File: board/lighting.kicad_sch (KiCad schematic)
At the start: 2 parts, among them U3 SHHD003A0A

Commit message: Fan, Light, Buck
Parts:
- removed Conn2: Molex_SL_03, MRDT_Connectors:MOLEX_SL_03_Vertical, symbol MRDT_Connectors:Molex_SL_03
- removed U3: SHHD003A0A, MRDT_Devices:SHHD003A0A41Z_Through_Hole, symbol MRDT_Devices:SHHD003A0A
- added Conn10: Molex_SL_03, symbol MRDT_Connectors:Molex_SL_03
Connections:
- net GND: now also Conn10.3
- net NeoPixel: now also Conn10.2
- new net +5V: Conn10.1
- no-connect marks 1 -> 0
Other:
- note removed: "NeoPixels"

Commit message: Added most Footprints, Schematic review touch up
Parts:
- Conn10: footprint (none) -> MRDT_Connectors:MOLEX_SL_04_Vertical
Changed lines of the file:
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@@
 			)
 		)
-		(property "Footprint" ""
+		(property "Footprint" "MRDT_Connectors:MOLEX_SL_04_Vertical"
 			(at 106.68 87.63 0)
 			(effects

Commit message: Layout edits
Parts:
- Conn10: footprint MRDT_Connectors:MOLEX_SL_04_Vertical -> MRDT_Connectors:MOLEX_SL_03_Vertical
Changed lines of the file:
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@@
 			)
 		)
-		(property "Footprint" "MRDT_Connectors:MOLEX_SL_04_Vertical"
+		(property "Footprint" "MRDT_Connectors:MOLEX_SL_03_Vertical"
 			(at 106.68 87.63 0)
 			(effects

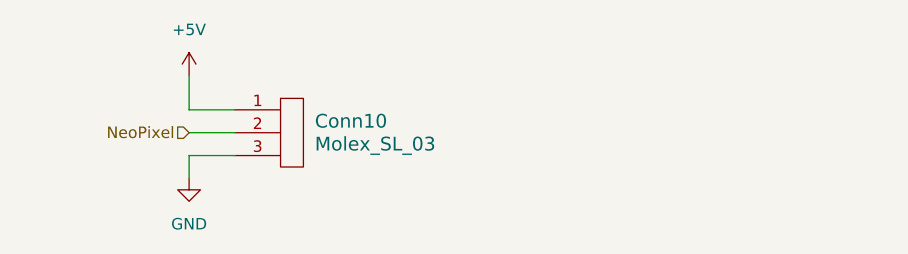
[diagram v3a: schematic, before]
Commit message: routed core board
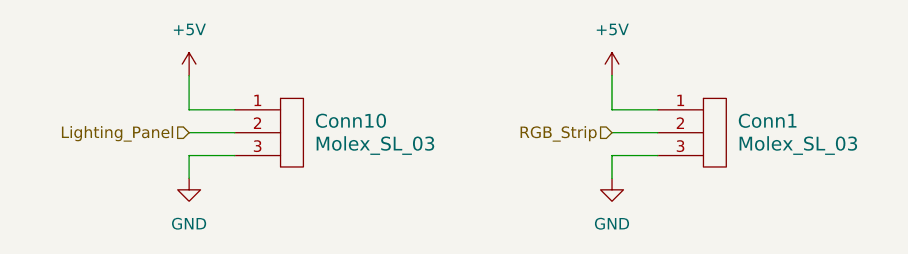
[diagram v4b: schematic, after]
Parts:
- added Conn1: Molex_SL_03, MRDT_Connectors:MOLEX_SL_03_Vertical, symbol MRDT_Connectors:Molex_SL_03
- Conn10: footprint MRDT_Connectors:MOLEX_SL_03_Vertical -> MRDT_Connectors:MOLEX_SL_03_Horizontal
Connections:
- net +5V: now also Conn1.1
- net GND: now also Conn1.3
- net NeoPixel renamed Lighting_Panel
- new net RGB_Strip: Conn1.2

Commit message: Cleaned up traces and silkscreens
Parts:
- Conn1: footprint MRDT_Connectors:MOLEX_SL_03_Vertical -> MRDT_Connectors:MOLEX_SL_03_Horizontal
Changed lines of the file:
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@@
 			)
 		)
-		(property "Footprint" "MRDT_Connectors:MOLEX_SL_03_Vertical"
+		(property "Footprint" "MRDT_Connectors:MOLEX_SL_03_Horizontal"
 			(at 153.67 87.63 0)
 			(effects

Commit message: rev2 progress
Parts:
- added Conn9: Molex_SL_04, MRDT_Connectors:MOLEX_SL_04_Horizontal, symbol MRDT_Connectors:Molex_SL_04
- added Q16, Q17, Q18: BSS138, Package_TO_SOT_SMD:SOT-23, symbol Transistor_FET:BSS138
- added R17, R19, R27: 10k, Resistor_SMD:R_0603_1608Metric_Pad0.98x0.95mm_HandSolder, symbol Device:R_US
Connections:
- net +5V: now also Conn9.1
- net GND: now also Q16.2 (S), Q17.2 (S), Q18.2 (S), R17.2, R19.2, R27.2
- new net: Conn9.3, Q17.3 (D)
- new net: Conn9.4, Q18.3 (D)
- new net: Conn9.2, Q16.3 (D)
- new net BStrip: Q18.1 (G), R27.1
- new net GStrip: Q17.1 (G), R19.1
- new net RStrip: Q16.1 (G), R17.1

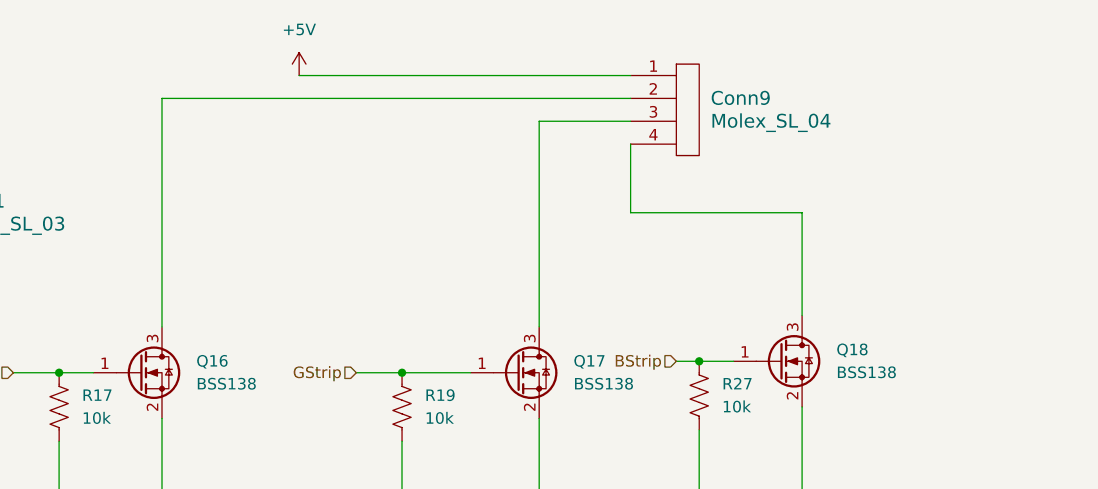
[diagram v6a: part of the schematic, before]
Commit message: move things for buck circuit
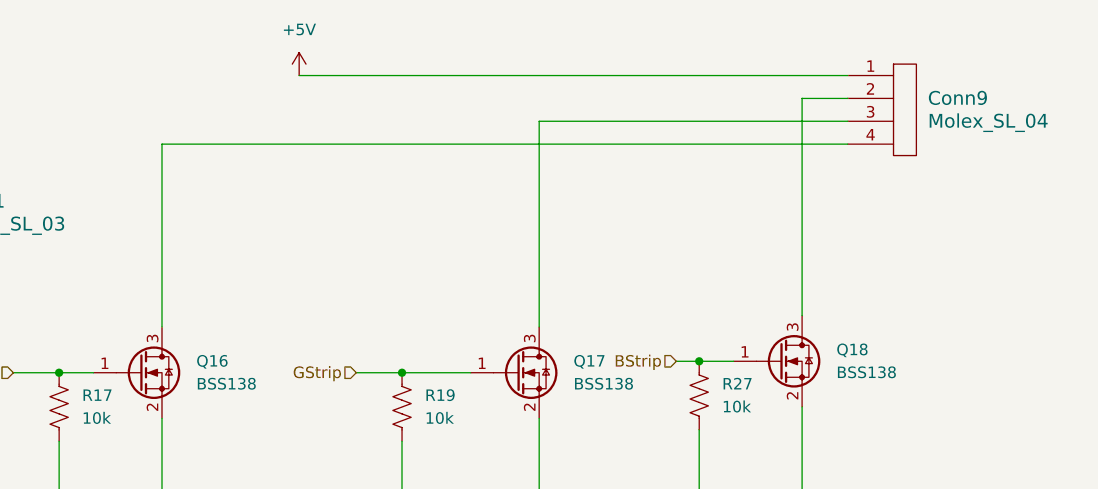
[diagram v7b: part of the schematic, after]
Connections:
- net at Q18.3 (D): now also Conn9.2; no longer Conn9.4
- net at Q16.3 (D): now also Conn9.4; no longer Conn9.2
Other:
- moved on the sheet: Conn9
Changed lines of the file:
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@@
+	(wire
+		(pts
+			(xy 257.81 71.12) (xy 252.73 71.12)
+		)
+		(stroke
+			(width 0)
+			(type default)
+		)
+	)
 	(wire
 		(pts
@@
 	(wire
 		(pts
+			(xy 181.61 76.2) (xy 257.81 76.2)
+		)
+		(stroke
+			(width 0)
+			(type default)
+		)
+	)
+	(wire
+		(pts
 			(xy 96.52 81.28) (xy 96.52 77.47)
 		)
@@
 	(wire
 		(pts
-			(xy 223.52 73.66) (xy 233.68 73.66)
+			(xy 223.52 73.66) (xy 257.81 73.66)
 		)
 		(stroke
@@
 	(wire
 		(pts
-			(xy 233.68 83.82) (xy 252.73 83.82)
-		)
-		(stroke
-			(width 0)
-			(type default)
-		)
-	)
-	(wire
-		(pts
 			(xy 181.61 106.68) (xy 181.61 115.57)
 		)
@@
 	(wire
 		(pts
-			(xy 233.68 83.82) (xy 233.68 76.2)
-		)
-		(stroke
-			(width 0)
-			(type default)
-		)
-	)
-	(wire
-		(pts
-			(xy 196.85 68.58) (xy 233.68 68.58)
+			(xy 252.73 71.12) (xy 252.73 95.25)
+		)
+		(stroke
+			(width 0)
+			(type default)
+		)
+	)
+	(wire
+		(pts
+			(xy 196.85 68.58) (xy 257.81 68.58)
 		)
 		(stroke
@@
 	(wire
 		(pts
-			(xy 252.73 95.25) (xy 252.73 83.82)
-		)
-		(stroke
-			(width 0)
-			(type default)
-		)
-	)
-	(wire
-		(pts
 			(xy 143.51 88.9) (xy 143.51 86.36)
 		)
@@
 	(wire
 		(pts
-			(xy 181.61 71.12) (xy 233.68 71.12)
-		)
-		(stroke
-			(width 0)
-			(type default)
-		)
-	)
-	(wire
-		(pts
-			(xy 181.61 96.52) (xy 181.61 71.12)
+			(xy 181.61 96.52) (xy 181.61 76.2)
 		)
 		(stroke
@@
 	(symbol
 		(lib_id "MRDT_Connectors:Molex_SL_04")
-		(at 238.76 77.47 0)
+		(at 262.89 77.47 0)
 		(unit 1)
 		(exclude_from_sim no)
@@
 		(fields_autoplaced yes)
 		(property "Reference" "Conn9"
-			(at 242.57 71.1199 0)
+			(at 266.7 71.1199 0)
 			(effects
 				(font
@@
 		)
 		(property "Value" "Molex_SL_04"
-			(at 242.57 73.6599 0)
+			(at 266.7 73.6599 0)
 			(effects
 				(font
@@
 		)
 		(property "Footprint" "MRDT_Connectors:MOLEX_SL_04_Horizontal"
-			(at 238.76 77.47 0)
+			(at 262.89 77.47 0)
 			(effects
 				(font
@@
 		)
 		(property "Datasheet" ""
-			(at 238.76 77.47 0)
+			(at 262.89 77.47 0)
 			(effects
 				(font
@@
 		)
 		(property "Description" ""
-			(at 238.76 77.47 0)
-			(effects
-				(font
+			(at 262.89 77.47 0)
+			(effects
+				(font
